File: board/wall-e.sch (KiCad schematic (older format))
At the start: 49 parts, among them J1 Raspberry_Pi_2_3, J10 PCA9685, J11 VL53L0X, J12 VL53L0X, J13 VL53L0X, J14 MotorDrv2, J15 Motor2, J2 LogicPwr, J3 NoisyPwr, J4 SSD1351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

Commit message: Add IMU and power sensors.
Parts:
- added C12, C13: 0.1u, Capacitors_SMD:C_0805_HandSoldering, symbol C_Small
- added J16: IMU, Connectors_JST:JST_XH_B10B-XH-A_10x2.50mm_Straight, symbol Conn_01x10
- added J17, J18: INA219, Connectors_JST:JST_XH_B04B-XH-A_04x2.50mm_Straight, symbol Conn_01x04
- added R19, R20: 4k7, Resistors_SMD:R_0805_HandSoldering, symbol R
- added R21, R22: 1k5, Resistors_SMD:R_0805_HandSoldering, symbol R
- added U5: ISO1541, Housings_SOIC:SOIC-8_3.9x4.9mm_Pitch1.27mm, symbol ISO1541
- C1, C10, C11, C2, C3, C4, C6, C7, C8, C9: footprint (none) -> Capacitors_SMD:C_0805_HandSoldering
- C5: footprint (none) -> Capacitors_Tantalum_SMD:CP_Tantalum_Case-E_EIA-7260-38_Hand
- J1: footprint Pin_Headers:Pin_Header_Straight_2x20 -> Pin_Headers:Pin_Header_Straight_2x20_Pitch2.54mm
- J10: footprint (none) -> Connectors_JST:JST_XH_B06B-XH-A_06x2.50mm_Straight
- J11, J12, J13, J4, J7, J8, J9: footprint (none) -> Connectors_JST:JST_XH_B07B-XH-A_07x2.50mm_Straight
- J14, J5: footprint (none) -> Connectors_JST:JST_XH_B03B-XH-A_03x2.50mm_Straight
- J15, J6: footprint (none) -> Connectors_JST:JST_XH_B04B-XH-A_04x2.50mm_Straight
- J2, J3: footprint (none) -> Connectors_JST:JST_XH_B02B-XH-A_02x2.50mm_Straight
- R1, R10, R11, R12, R13, R14, R15, R16, R17, R18, R2, R3, R4, R5, R6, R7, R8, R9: footprint (none) -> Resistors_SMD:R_0805_HandSoldering
- U1: footprint Package_QFP:LQFP-44_10x10mm_P0.8mm -> Housings_QFP:LQFP-44_10x10mm_Pitch0.8mm
- U3, U4: footprint (none) -> Housings_SOIC:SOIC-16W_7.5x10.3mm_Pitch1.27mm
- Y1: footprint (none) -> Crystals:Crystal_SMD_HC49-SD_HandSoldering
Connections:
- net labels added: I2C_ISO_SCL, I2C_ISO_SDA, PI_SPI1_MISO, PI_SPI1_MOSI, PI_SPI1_SCLK
- wire segments 282 -> 330
- no-connect marks 20 -> 24
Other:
- note added: "0-5: ToFs\n"
- note added: "6: Isolated I2C"
- note added: "7: Prop"
- note added: "Battery sensors\nDifferent addresses!"
- note added: "SCREEN\n"
- note added: "Vcc\nGND\nSCL\nSDA"
- note added: "Vcc\nGND\nSCL\nSDA/SDI\nEDA\nECL\nADO/SDO\nINT\nNCS\nFSYNC"
- moved on the sheet: C1, C10, C11, C2, C3, C4, C5, C6, C7, C8, C9, J10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

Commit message: Start to group components on board.
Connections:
- wire segments 330 -> 331
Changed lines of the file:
@@
 LIBS:contrib
 LIBS:valves
+LIBS:lm2576
+LIBS:iso1541
+LIBS:iso7742
 LIBS:MCU_Parallax
-LIBS:iso7742
-LIBS:iso1541
 LIBS:wall-e-cache
 EELAYER 25 0
@@
 Wire Wire Line
 	8950 6250 9000 6250
-Text Notes 7800 5750 0    60   ~ 0
+Text Notes 7750 5750 0    60   ~ 0
 Battery sensors\nDifferent addresses!
+Wire Wire Line
+	7750 4450 7750 4300
 $EndSCHEMATC

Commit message: More routing; add Pi outline.
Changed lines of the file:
@@
 Connection ~ 4550 4900
-Wire Wire Line
-	4800 5250 4800 5400
 Wire Wire Line
 	4800 5400 4550 5400
@@
 Wire Wire Line
 	7750 4450 7750 4300
+Wire Wire Line
+	4800 5400 4800 5300
 $EndSCHEMATC

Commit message: Smaller board
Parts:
- removed J11, J12, J13, J7, J8, J9: VL53L0X, Connectors_JST:JST_XH_B07B-XH-A_07x2.50mm_Straight, symbol Conn_01x07
- removed J16: IMU, Connectors_JST:JST_XH_B10B-XH-A_10x2.50mm_Straight, symbol Conn_01x10
- added J11, J12, J13, J7, J8, J9: VL53L0X, Connectors_JST:JST_XH_B04B-XH-A_04x2.50mm_Straight, symbol Conn_01x04
- added J16: IMU, Connectors_JST:JST_XH_B06B-XH-A_06x2.50mm_Straight, symbol Conn_01x06
- J1: footprint Pin_Headers:Pin_Header_Straight_2x20_Pitch2.54mm -> Socket_Strips:Socket_Strip_Straight_2x20_Pitch2.54mm
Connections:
- wire segments 331 -> 349
- no-connect marks 24 -> 2
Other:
- note added: "Vcc\nGND\nSCL\nSDA/SDI\nADO/SDO\nNCS"
- note added: "Vin\nGND\nSCL\nSDA"
- note removed: "Vcc\nGND\nSCL\nSDA/SDI\nEDA\nECL\nADO/SDO\nINT\nNCS\nFSYNC"
- note removed: "Vin\n2.8V out\nGND\nGPIO\nXSHUT\nSCL\nSDA"

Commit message: Tweaks
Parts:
- added J19: GS2, Connectors:GS2, symbol GS2
- added J20: SDA, symbol TEST_1P
- added J21: SCL, symbol TEST_1P
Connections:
- net GND: now also J19.2 (G2)
- net GNDA: now also J19.1 (G1)
- net PI_I2C_SCLK: now also J21.1
- net PI_I2C_SDA: now also J20.1

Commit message: Swap in through-hole cap
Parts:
- C5: footprint Capacitors_Tantalum_SMD:CP_Tantalum_Case-E_EIA-7260-38_Hand -> Capacitors_THT:CP_Radial_D8.0mm_P3.50mm
- J20, J21: footprint (none) -> Connectors:1pin

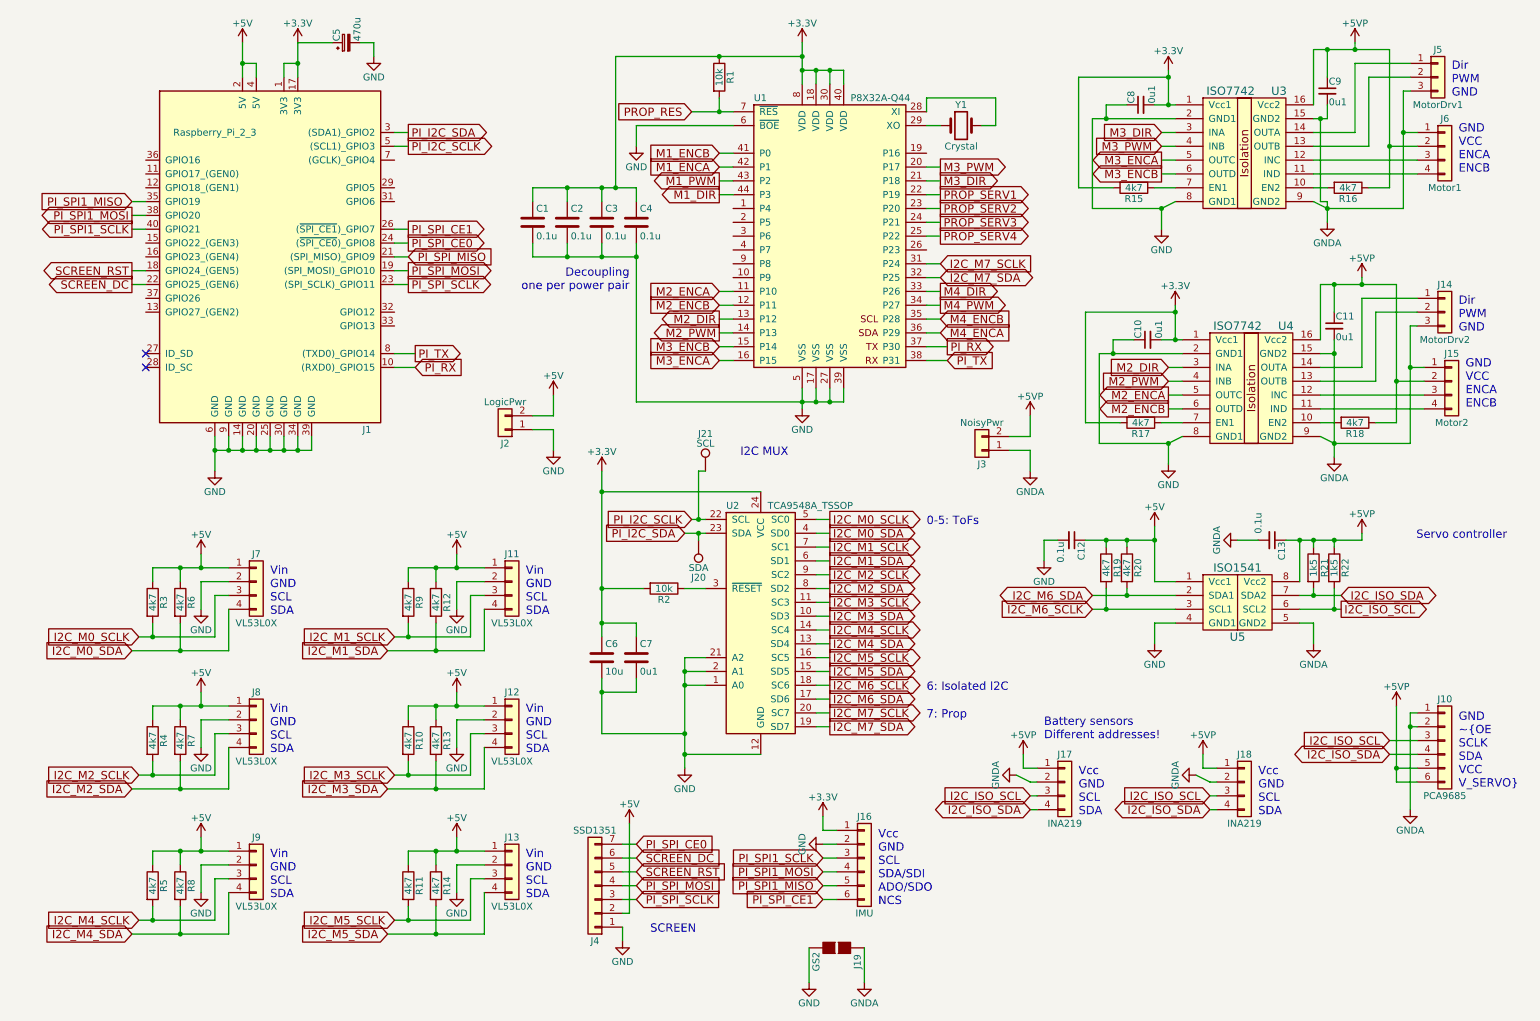
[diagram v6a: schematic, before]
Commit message: Move board over ports and re-route.
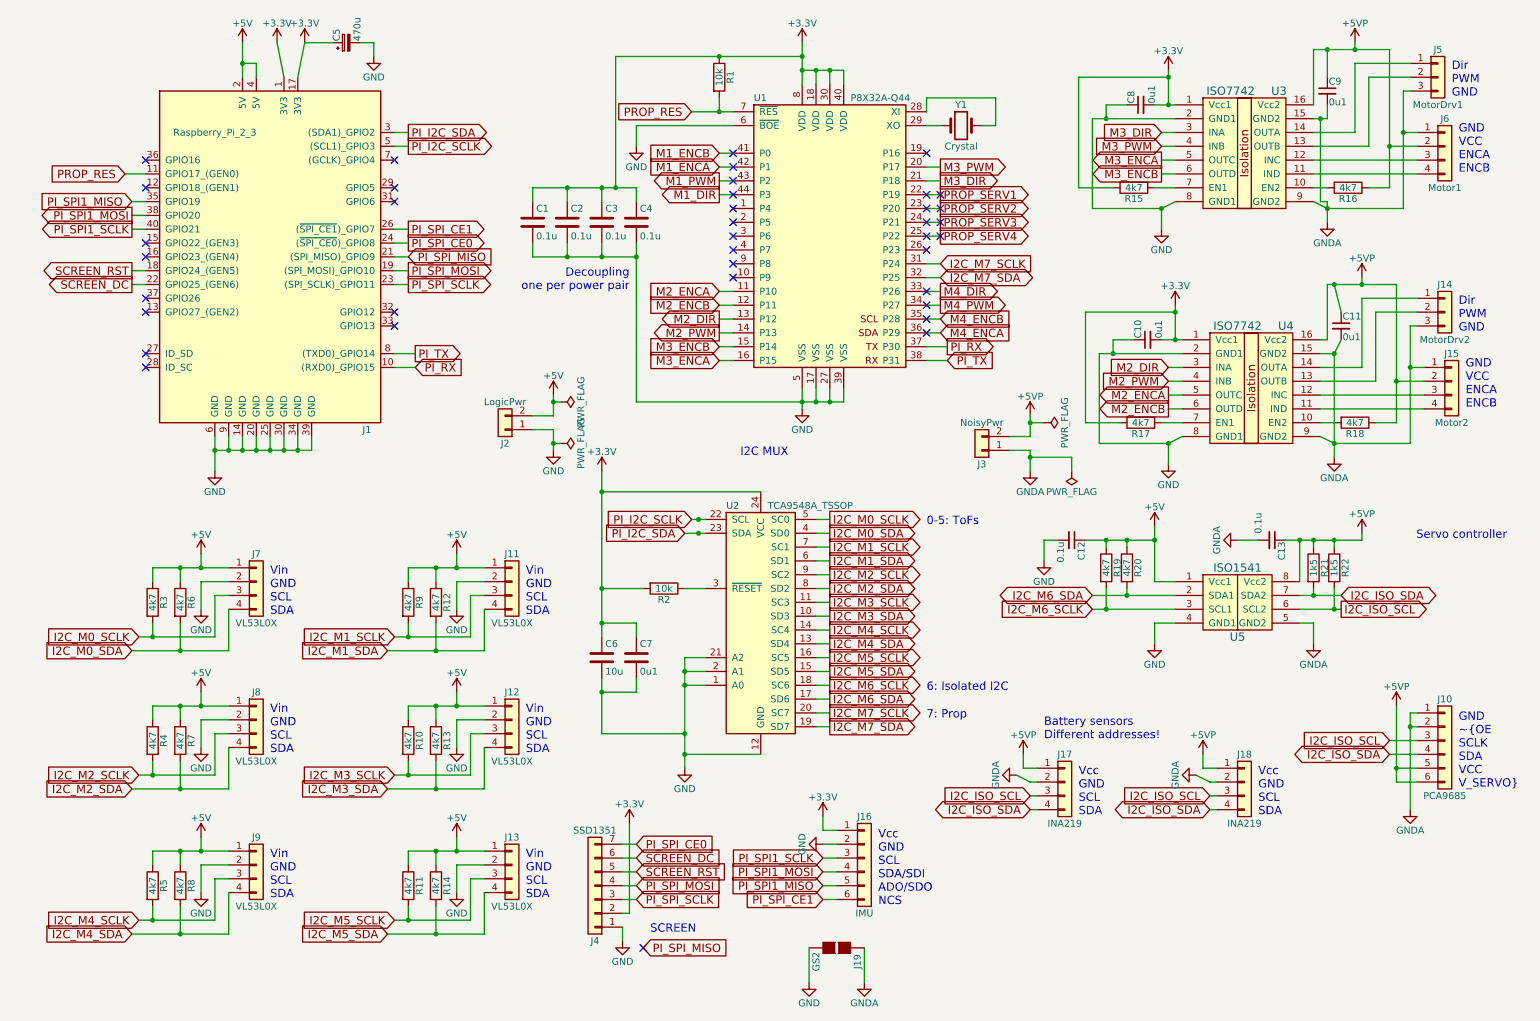
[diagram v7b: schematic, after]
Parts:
- removed J20: SDA, Connectors:1pin, symbol TEST_1P
- removed J21: SCL, Connectors:1pin, symbol TEST_1P
- C6: footprint Capacitors_SMD:C_0805_HandSoldering -> Capacitors_Tantalum_SMD:CP_Tantalum_Case-C_EIA-6032-28_Hand
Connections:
- net +3V3: now also J4.2 (Pin_2)
- net +5V: no longer J4.2 (Pin_2)
- net PROP_RES: now also J1.11 (GPIO17_(GEN0))
- no-connect marks 2 -> 38
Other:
- moved on the sheet: C11
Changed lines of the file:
@@
-$EndComp
-$Comp
-L +5V #PWR02
-U 1 1 5B5C7E54
-P 4750 6350
-F 0 "#PWR02" H 4750 6200 50  0001 C CNN
-F 1 "+5V" H 4750 6490 50  0000 C CNN
-F 2 "" H 4750 6350 50  0001 C CNN
-F 3 "" H 4750 6350 50  0001 C CNN
-	1    4750 6350
-	1    0    0    -1
 $EndComp
 $Comp
@@
 F 0 "C6" H 4575 5250 50  0000 L CNN
 F 1 "10u" H 4575 5050 50  0000 L CNN
-F 2 "Capacitors_SMD:C_0805_HandSoldering" H 4588 5000 50  0001 C CNN
+F 2 "Capacitors_Tantalum_SMD:CP_Tantalum_Case-C_EIA-6032-28_Hand" H 4588 5000 50  0001 C CNN
 F 3 "" H 4550 5150 50  0001 C CNN
 	1    4550 5150
@@
 L +3.3V #PWR024
 U 1 1 5B636B1C
-P 2350 700
-F 0 "#PWR024" H 2350 550 50  0001 C CNN
-F 1 "+3.3V" H 2350 840 50  0000 C CNN
-F 2 "" H 2350 700 50  0001 C CNN
-F 3 "" H 2350 700 50  0001 C CNN
-	1    2350 700
+P 2400 700
+F 0 "#PWR024" H 2400 550 50  0001 C CNN
+F 1 "+3.3V" H 2400 840 50  0000 C CNN
+F 2 "" H 2400 700 50  0001 C CNN
+F 3 "" H 2400 700 50  0001 C CNN
+	1    2400 700
 	1    0    0    -1
 $EndComp
@@
 L C_Small C11
 U 1 1 5B6558C3
-P 9850 2750
-F 0 "C11" H 9860 2820 50  0000 L CNN
-F 1 "0u1" H 9860 2670 50  0000 L CNN
-F 2 "Capacitors_SMD:C_0805_HandSoldering" H 9850 2750 50  0001 C CNN
-F 3 "" H 9850 2750 50  0001 C CNN
-	1    9850 2750
+P 9900 2750
+F 0 "C11" H 9910 2820 50  0000 L CNN
+F 1 "0u1" H 9910 2670 50  0000 L CNN
+F 2 "Capacitors_SMD:C_0805_HandSoldering" H 9900 2750 50  0001 C CNN
+F 3 "" H 9900 2750 50  0001 C CNN
+	1    9900 2750
 	1    0    0    -1
 $EndComp
@@
 	9850 3600 9750 3550
 Wire Wire Line
-	9850 3600 10400 3600
-Wire Wire Line
-	10400 3600 10400 2750
+	10400 3600 9850 3600
+Wire Wire Line
+	10400 2750 10400 3600
 Wire Wire Line
 	10500 3050 10400 3050
 Wire Wire Line
-	9850 2850 9850 3700
-Wire Wire Line
-	9750 2950 9850 2950
+	9900 2850 9850 2950
+Wire Wire Line
+	9850 2950 9850 3700
+Wire Wire Line
+	9850 2950 9750 2950
 Connection ~ 9850 2450
 Wire Wire Line
-	9850 2650 9850 2450
+	9900 2650 9850 2450
 Wire Wire Line
 	10300 3150 10500 3150
@@
 	10300 2450 10300 3450
 Wire Wire Line
-	9750 2450 10300 2450
-Wire Wire Line
-	9750 2850 9750 2450
+	9800 2450 10300 2450
+Wire Wire Line
+	9800 2850 9800 2450
 Connection ~ 9850 3600
 Wire Wire Line
@@
 	9800 1850 9800 2000
 Wire Wire Line
-	2600 700  2350 700
-Connection ~ 2350 850
-Wire Wire Line
-	2250 850  2350 850
-Wire Wire Line
-	2250 950  2250 850
-Wire Wire Line
-	2350 700  2350 950
+	2600 700  2400 700
+Wire Wire Line
+	2400 700  2350 950
 Wire Wire Line
 	4200 3500 4200 3650
@@
 Wire Wire Line
 	6450 7250 6450 7500
-$Comp
-L TEST_1P J20
-U 1 1 5BF33E1C
-P 5250 4300
-F 0 "J20" H 5250 4570 50  0000 C CNN
-F 1 "SDA" H 5250 4500 50  0000 C CNN
-F 2 "Connectors:1pin" H 5450 4300 50  0001 C CNN
-F 3 "" H 5450 4300 50  0001 C CNN
-	1    5250 4300
+Connection ~ 5250 4150
+Connection ~ 5250 4250
+Wire Wire Line
+	9750 2850 9800 2850
+$Comp
+L PWR_FLAG #FLG052
+U 1 1 5C026CFB
+P 7750 3450
+F 0 "#FLG052" H 7750 3525 50  0001 C CNN
+F 1 "PWR_FLAG" H 7750 3600 50  0000 C CNN
+F 2 "" H 7750 3450 50  0001 C CNN
+F 3 "" H 7750 3450 50  0001 C CNN
+	1    7750 3450
+	0    1    1    0
+$EndComp
+Wire Wire Line
+	7750 3450 7650 3450
+Connection ~ 7650 3450
+Wire Wire Line
+	7950 3800 7950 3700
+Wire Wire Line
+	7950 3700 7650 3700
+Connection ~ 7650 3700
+$Comp
+L PWR_FLAG #FLG053
+U 1 1 5C027A7F
+P 7950 3800
+F 0 "#FLG053" H 7950 3875 50  0001 C CNN
+F 1 "PWR_FLAG" H 7950 3950 50  0000 C CNN
+F 2 "" H 7950 3800 50  0001 C CNN
+F 3 "" H 7950 3800 50  0001 C CNN
+	1    7950 3800
 	-1   0    0    1
 $EndComp
 $Comp
-L TEST_1P J21
-U 1 1 5BF33EF9
-P 5300 3800
-F 0 "J21" H 5300 4070 50  0000 C CNN
-F 1 "SCL" H 5300 4000 50  0000 C CNN
-F 2 "Connectors:1pin" H 5500 3800 50  0001 C CNN
-F 3 "" H 5500 3800 50  0001 C CNN
-	1    5300 3800
-	1    0    0    -1
-$EndComp
-Wire Wire Line
-	5300 3800 5250 3800
-Wire Wire Line
-	5250 3800 5250 4150
-Connection ~ 5250 4150
-Wire Wire Line
-	5250 4300 5250 4250
-Connection ~ 5250 4250
+L PWR_FLAG #FLG054
+U 1 1 5C027C73
+P 4250 3600
+F 0 "#FLG054" H 4250 3675 50  0001 C CNN
+F 1 "PWR_FLAG" H 4250 3750 50  0000 C CNN
+F 2 "" H 4250 3600 50  0001 C CNN
+F 3 "" H 4250 3600 50  0001 C CNN
+	1    4250 3600
+	0    1    1    0
+$EndComp
+$Comp
+L PWR_FLAG #FLG055
+U 1 1 5C027CFF
+P 4250 3300
+F 0 "#FLG055" H 4250 3375 50  0001 C CNN
+F 1 "PWR_FLAG" H 4250 3450 50  0000 C CNN
+F 2 "" H 4250 3300 50  0001 C CNN
+F 3 "" H 4250 3300 50  0001 C CNN
+	1    4250 3300
+	0    1    1    0
+$EndComp
+Wire Wire Line
+	4250 3300 4200 3300
+Connection ~ 4200 3300
+Wire Wire Line
+	4250 3600 4200 3600
+Connection ~ 4200 3600
+NoConn ~ 6900 1500
+NoConn ~ 5500 2400
+NoConn ~ 5500 2300
+NoConn ~ 5500 2200
+NoConn ~ 5500 2100
+NoConn ~ 5500 2000
+NoConn ~ 5500 1900
+NoConn ~ 5500 1800
+NoConn ~ 5500 1700
+NoConn ~ 5500 1600
+NoConn ~ 5500 1500
+NoConn ~ 3050 1850
+NoConn ~ 3050 1750
+NoConn ~ 3050 1550
+NoConn ~ 3050 2650
+NoConn ~ 3050 2750
+NoConn ~ 1250 2650
+NoConn ~ 1250 2550
+NoConn ~ 1250 2250
+NoConn ~ 1250 2150
+NoConn ~ 1250 1750
+NoConn ~ 1250 1550
+Text GLabel 4850 7250 2    60   Input ~ 0
+PI_SPI_MISO
+NoConn ~ 4850 7250
+NoConn ~ 6900 2200
+NoConn ~ 7000 2100
+NoConn ~ 7000 2000
+NoConn ~ 7000 1900
+NoConn ~ 7000 1800
+NoConn ~ 6900 1800
+NoConn ~ 6900 1900
+NoConn ~ 6900 2000
+NoConn ~ 6900 2100
+NoConn ~ 6900 2500
+NoConn ~ 6900 2600
+NoConn ~ 6900 2700
+NoConn ~ 6900 2800
+$Comp
+L +3.3V #PWR056
+U 1 1 5C02CA19
+P 2200 700
+F 0 "#PWR056" H 2200 550 50  0001 C CNN
+F 1 "+3.3V" H 2200 840 50  0000 C CNN
+F 2 "" H 2200 700 50  0001 C CNN
+F 3 "" H 2200 700 50  0001 C CNN
+	1    2200 700
+	1    0    0    -1
+$EndComp
+Wire Wire Line
+	2250 950  2200 700
+Text GLabel 1100 1650 0    60   Input ~ 0
+PROP_RES
+Wire Wire Line
+	1250 1650 1100 1650
+$Comp
+L +3.3V #PWR?
+U 1 1 5C027A8A
+P 4750 6350
+F 0 "#PWR?" H 4750 6200 50  0001 C CNN
+F 1 "+3.3V" H 4750 6490 50  0000 C CNN
+F 2 "" H 4750 6350 50  0001 C CNN
+F 3 "" H 4750 6350 50  0001 C CNN
+	1    4750 6350
+	1    0    0    -1
+$EndComp
 $EndSCHEMATC

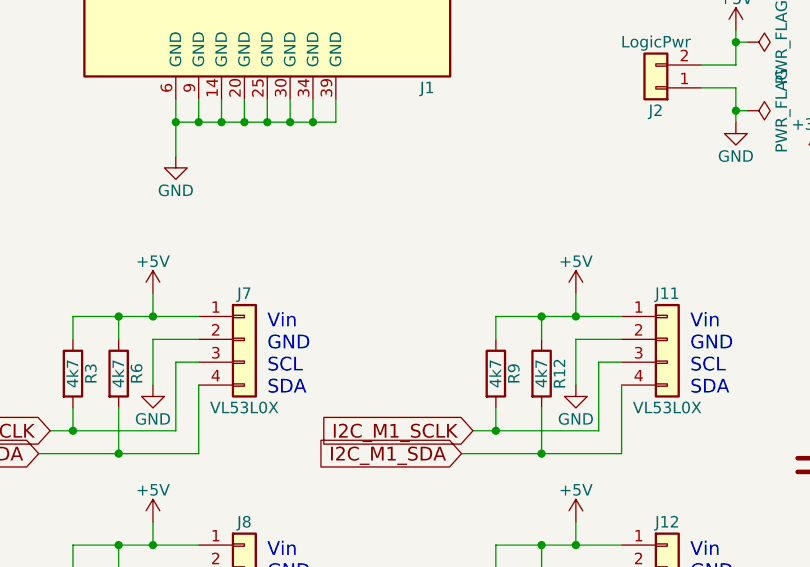
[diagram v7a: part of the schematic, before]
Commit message: Tweaks: add cap and fill.
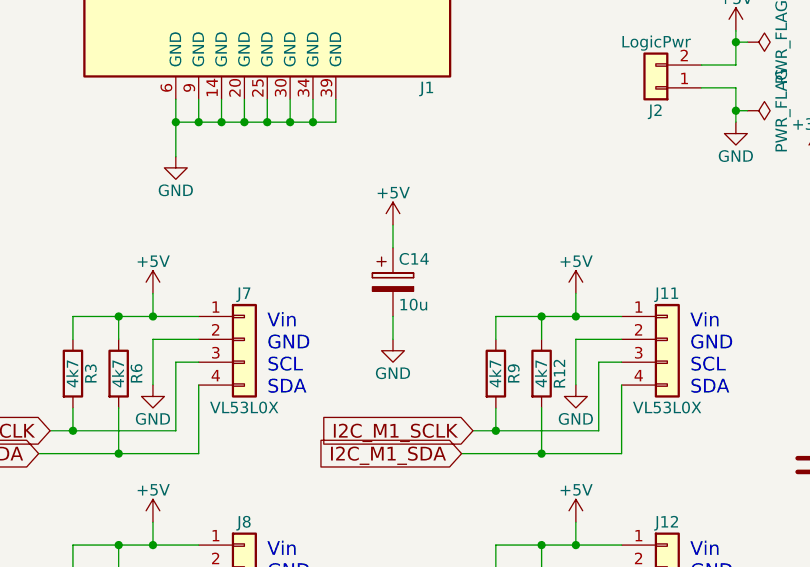
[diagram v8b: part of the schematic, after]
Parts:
- added C14: 10u, Capacitors_Tantalum_SMD:CP_Tantalum_Case-C_EIA-6032-28_Hand, symbol CP
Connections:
- net +5V: now also C14.1
- net GND: now also C14.2
